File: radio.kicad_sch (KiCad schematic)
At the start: 0 parts

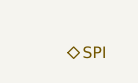
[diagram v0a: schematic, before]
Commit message: Fixed bus names
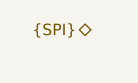
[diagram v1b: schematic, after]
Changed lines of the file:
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@@
 (kicad_sch (version 20211123) (generator eeschema)
   (paper "A4")
-  (hierarchical_label "SPI" (shape bidirectional) (at 25.4 31.75 0)
-    (effects (font (size 1.27 1.27)) (justify left))
+  (hierarchical_label "{SPI}" (shape bidirectional) (at 27.94 29.21 180)
+    (effects (font (size 1.27 1.27)) (justify right))
   )
 )

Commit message: Various updates because I forgot to commit for a while
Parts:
- added AE1: Antenna, Connector_Coaxial:SMA_Molex_73251-2200_Horizontal, symbol Device:Antenna
- added C20: 5.1p, symbol Device:C
- added CM1: 6.8n, symbol Device:L
- added CM2, CM3: 3.3p, symbol Device:C
- added CR1: 3p, symbol Device:C
- added CR2: 1.2p, symbol Device:C
- added L1: 3.3n, symbol Device:L
- added LM1, LM3: 12n, symbol Device:L
- added LM2, LR2: 24n, symbol Device:L
- added LR1: 18n, symbol Device:L
- added Lc1: 120n, symbol Device:L
- added U8: Si4468/7, symbol YAR_Comms:Si4468/7
- added Y2: 30MHz, symbol Device:Crystal
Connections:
- new net: AE1.1 (A), LM3.1
- new net: CM3.1, LM2.1, LM3.2
- new net: CM2.1, LM1.1, LM2.2
- new net: CR1.1, LR1.1, LR2.2, U8.3 (RXn)
- new net: C20.2, Lc1.2, U8.4 (TX)
- new net: C20.1, L1.1
- new net: CM1.2, CR2.2, L1.2, LM1.2, LR2.1
- new net: CR2.1, LR1.2, U8.2 (RXp)
- new net: U8.16 (XOUT), Y2.1
- new net: U8.17 (XIN), Y2.2
- new net +3V3: Lc1.1, U8.6 (Vcc), U8.8 (Vcc)
- new net CS1: U8.15 (CS)
- new net GND: CM1.1, CM2.2, CM3.2, CR1.2, U8.1 (SDN), U8.18 (GND), U8.21 (GND), U8.5 (GND)
- new net Radio: U8.11 (~{IRQ})
- new net Rx: U8.13 (SDO)
- new net SCK: U8.12 (SCLK)
- new net Tx: U8.14 (SDI)
- no-connect marks 0 -> 5
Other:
- note added: "CM is actually an inductor because reasons. I hate it too."
- title: (none) -> Pheonix Radio

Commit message: Added footprint
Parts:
- Y2: footprint (none) -> Oscillator:Oscillator_SMD_Abracon_ASE-4Pin_3.2x2.5mm
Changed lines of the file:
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@@
       (effects (font (size 1.27 1.27)) (justify right))
     )
-    (property "Footprint" "" (id 2) (at 59.69 73.66 0)
+    (property "Footprint" "Oscillator:Oscillator_SMD_Abracon_ASE-4Pin_3.2x2.5mm" (id 2) (at 59.69 73.66 0)
       (effects (font (size 1.27 1.27)) hide)
     )

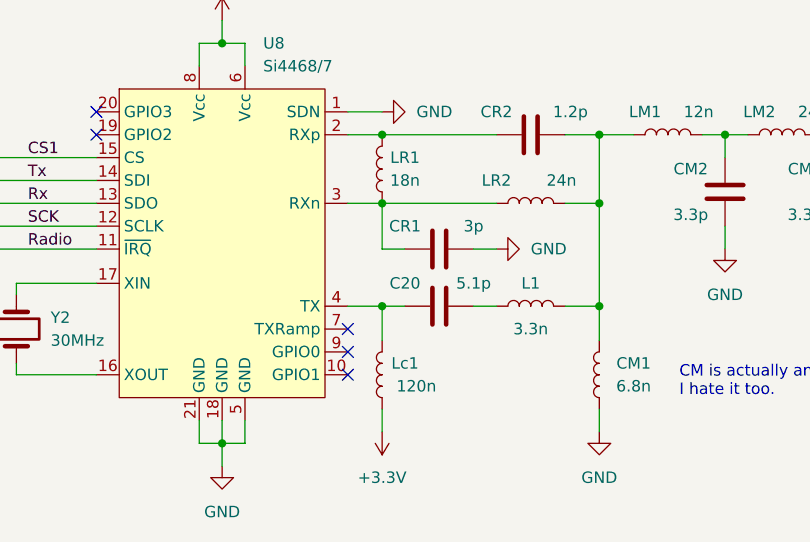
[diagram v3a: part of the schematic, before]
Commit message: Connected the sensors, flash chip, Need to connect the radio and GPS
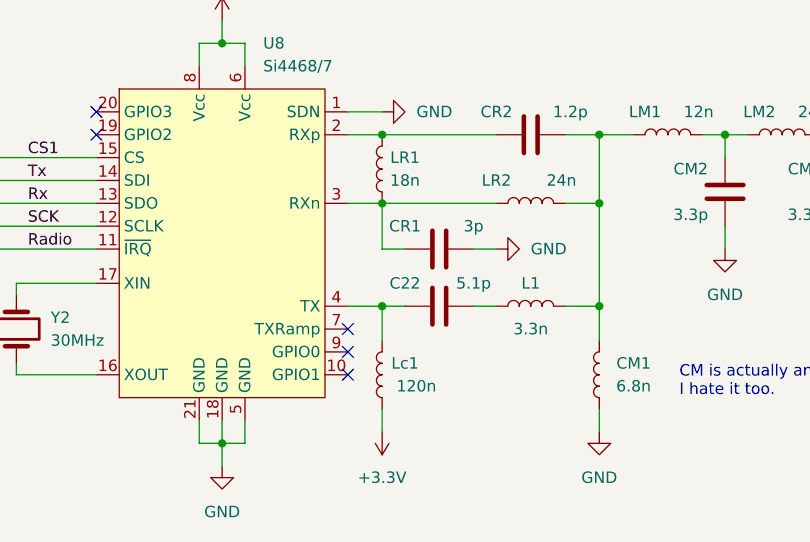
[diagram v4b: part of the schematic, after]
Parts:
- U8: footprint (none) -> YAR_RF:SI4468-A2A-IMR
- renumbered C20 to C22
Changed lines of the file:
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@@
   (symbol (lib_id "power:GND") (at 100.33 49.53 90) (unit 1)
     (in_bom yes) (on_board yes) (fields_autoplaced)
-    (property "Reference" "#PWR045" (id 0) (at 106.68 49.53 0)
+    (property "Reference" "#PWR047" (id 0) (at 106.68 49.53 0)
       (effects (font (size 1.27 1.27)) hide)
     )
@@
   (symbol (lib_id "power:GND") (at 151.13 64.77 0) (unit 1)
     (in_bom yes) (on_board yes) (fields_autoplaced)
-    (property "Reference" "#PWR050" (id 0) (at 151.13 71.12 0)
+    (property "Reference" "#PWR052" (id 0) (at 151.13 71.12 0)
       (effects (font (size 1.27 1.27)) hide)
     )
@@
   (symbol (lib_id "Device:C") (at 106.68 71.12 270) (mirror x) (unit 1)
     (in_bom yes) (on_board yes)
-    (property "Reference" "C20" (id 0) (at 102.87 68.58 90))
+    (property "Reference" "C22" (id 0) (at 102.87 68.58 90))
     (property "Value" "5.1p" (id 1) (at 110.49 68.58 90))
     (property "Footprint" "" (id 2) (at 102.87 70.1548 0)
@@
   (symbol (lib_id "power:GND") (at 138.43 64.77 0) (unit 1)
     (in_bom yes) (on_board yes) (fields_autoplaced)
-    (property "Reference" "#PWR049" (id 0) (at 138.43 71.12 0)
+    (property "Reference" "#PWR051" (id 0) (at 138.43 71.12 0)
       (effects (font (size 1.27 1.27)) hide)
     )
@@
   (symbol (lib_id "power:+3.3V") (at 82.55 39.37 0) (unit 1)
     (in_bom yes) (on_board yes) (fields_autoplaced)
-    (property "Reference" "#PWR043" (id 0) (at 82.55 43.18 0)
+    (property "Reference" "#PWR045" (id 0) (at 82.55 43.18 0)
       (effects (font (size 1.27 1.27)) hide)
     )
@@
   (symbol (lib_id "power:GND") (at 124.46 85.09 0) (unit 1)
     (in_bom yes) (on_board yes) (fields_autoplaced)
-    (property "Reference" "#PWR048" (id 0) (at 124.46 91.44 0)
+    (property "Reference" "#PWR050" (id 0) (at 124.46 91.44 0)
       (effects (font (size 1.27 1.27)) hide)
     )
@@
   (symbol (lib_id "power:+3.3V") (at 100.33 85.09 180) (unit 1)
     (in_bom yes) (on_board yes) (fields_autoplaced)
-    (property "Reference" "#PWR046" (id 0) (at 100.33 81.28 0)
+    (property "Reference" "#PWR048" (id 0) (at 100.33 81.28 0)
       (effects (font (size 1.27 1.27)) hide)
     )
@@
       (effects (font (size 1.27 1.27)) (justify left))
     )
-    (property "Footprint" "" (id 2) (at 82.55 58.42 0)
+    (property "Footprint" "YAR_RF:SI4468-A2A-IMR" (id 2) (at 82.55 58.42 0)
       (effects (font (size 1.27 1.27)) hide)
     )
@@
   (symbol (lib_id "power:GND") (at 82.55 88.9 0) (unit 1)
     (in_bom yes) (on_board yes) (fields_autoplaced)
-    (property "Reference" "#PWR044" (id 0) (at 82.55 95.25 0)
+    (property "Reference" "#PWR046" (id 0) (at 82.55 95.25 0)
       (effects (font (size 1.27 1.27)) hide)
     )
@@
   (symbol (lib_id "power:GND") (at 113.03 64.77 90) (unit 1)
     (in_bom yes) (on_board yes) (fields_autoplaced)
-    (property "Reference" "#PWR047" (id 0) (at 119.38 64.77 0)
-      (effects (font (size 1.27 1.27)) hide)
-    )
+    (property "Reference" "#PWR049" (id 0) (at 119.38 64.77 0)
+      (effects (font (size 1.27 1.27)) hide)
+    )

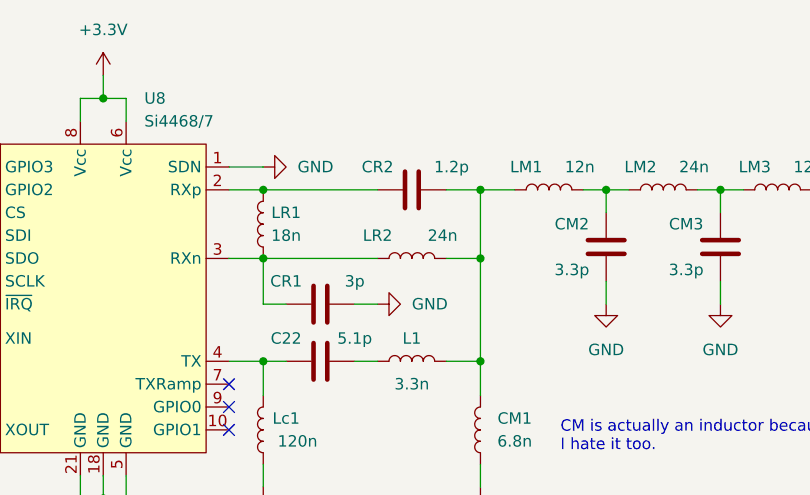
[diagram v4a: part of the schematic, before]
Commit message: Rearrange parts of PCB
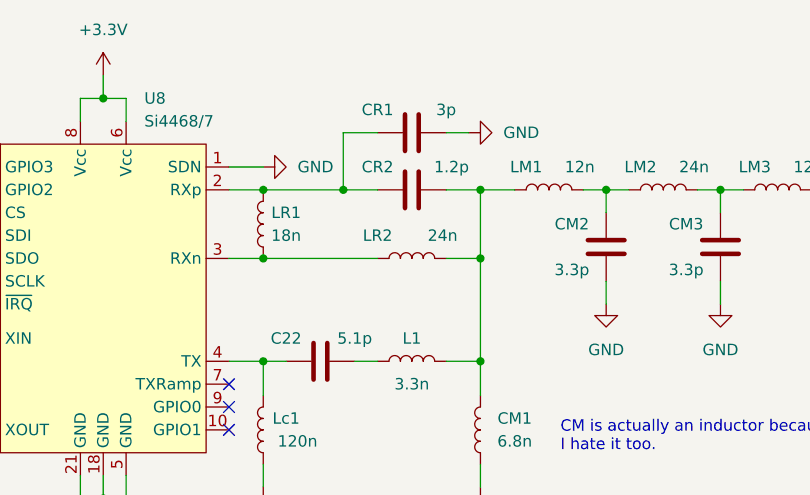
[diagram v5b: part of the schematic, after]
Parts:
- C22, CM1, CM2, CM3, CR1, CR2: footprint (none) -> Capacitor_SMD:C_0603_1608Metric
- L1, LM1, LM2, LM3, LR1, LR2, Lc1: footprint (none) -> Inductor_SMD:L_0603_1608Metric
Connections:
- net at LR1.1, LR2.2, U8.3 (RXn): no longer CR1.1
- net at CR2.1, LR1.2, U8.2 (RXp): now also CR1.1
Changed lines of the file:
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@@
   (junction (at 82.55 86.36) (diameter 0) (color 0 0 0 0)
+  )
+  (junction (at 109.22 52.07) (diameter 0) (color 0 0 0 0)
   )
   (no_connect (at 96.52 78.74))
@@
     (stroke (width 0) (type default) (color 0 0 0 0))
   )
+  (wire (pts (xy 109.22 52.07) (xy 113.03 52.07))
+    (stroke (width 0) (type default) (color 0 0 0 0))
+  )
   (wire (pts (xy 96.52 49.53) (xy 100.33 49.53))
     (stroke (width 0) (type default) (color 0 0 0 0))
@@
     (stroke (width 0) (type default) (color 0 0 0 0))
   )
-  (wire (pts (xy 100.33 52.07) (xy 113.03 52.07))
+  (wire (pts (xy 100.33 52.07) (xy 109.22 52.07))
+    (stroke (width 0) (type default) (color 0 0 0 0))
+  )
+  (wire (pts (xy 109.22 45.72) (xy 113.03 45.72))
     (stroke (width 0) (type default) (color 0 0 0 0))
   )
@@
     (stroke (width 0) (type default) (color 0 0 0 0))
   )
+  (wire (pts (xy 120.65 45.72) (xy 123.19 45.72))
+    (stroke (width 0) (type default) (color 0 0 0 0))
+  )
   (wire (pts (xy 80.01 44.45) (xy 80.01 41.91))
     (stroke (width 0) (type default) (color 0 0 0 0))
   )
-  (wire (pts (xy 100.33 59.69) (xy 100.33 64.77))
-    (stroke (width 0) (type default) (color 0 0 0 0))
-  )
   (wire (pts (xy 96.52 59.69) (xy 100.33 59.69))
     (stroke (width 0) (type default) (color 0 0 0 0))
@@
     (stroke (width 0) (type default) (color 0 0 0 0))
   )
-  (wire (pts (xy 110.49 64.77) (xy 113.03 64.77))
-    (stroke (width 0) (type default) (color 0 0 0 0))
-  )
   (wire (pts (xy 59.69 68.58) (xy 59.69 69.85))
     (stroke (width 0) (type default) (color 0 0 0 0))
@@
     (stroke (width 0) (type default) (color 0 0 0 0))
   )
+  (wire (pts (xy 109.22 45.72) (xy 109.22 52.07))
+    (stroke (width 0) (type default) (color 0 0 0 0))
+  )
   (wire (pts (xy 57.15 59.69) (xy 68.58 59.69))
     (stroke (width 0) (type default) (color 0 0 0 0))
@@
   )
   (bus (pts (xy 50.8 67.31) (xy 54.61 67.31))
-    (stroke (width 0) (type default) (color 0 0 0 0))
-  )
-  (wire (pts (xy 100.33 64.77) (xy 102.87 64.77))
     (stroke (width 0) (type default) (color 0 0 0 0))
   )
@@
     (effects (font (size 1.27 1.27)) (justify right))
   )
+  (symbol (lib_id "Device:C") (at 116.84 45.72 90) (mirror x) (unit 1)
+    (in_bom yes) (on_board yes)
+    (property "Reference" "CR1" (id 0) (at 113.03 43.18 90))
+    (property "Value" "3p" (id 1) (at 120.65 43.18 90))
+    (property "Footprint" "Capacitor_SMD:C_0603_1608Metric" (id 2) (at 120.65 46.6852 0)
+      (effects (font (size 1.27 1.27)) hide)
+    )
+    (property "Datasheet" "~" (id 3) (at 116.84 45.72 0)
+      (effects (font (size 1.27 1.27)) hide)
+    )
+    (pin "1")
+    (pin "2")
+  )
   (symbol (lib_id "Device:Antenna") (at 163.83 44.45 0) (unit 1)
     (in_bom yes) (on_board yes) (fields_autoplaced)
@@
       (effects (font (size 1.27 1.27)) (justify right))
     )
-    (property "Footprint" "" (id 2) (at 144.78 52.07 0)
+    (property "Footprint" "Inductor_SMD:L_0603_1608Metric" (id 2) (at 144.78 52.07 0)
       (effects (font (size 1.27 1.27)) hide)
     )
     (property "Datasheet" "~" (id 3) (at 144.78 52.07 0)
-      (effects (font (size 1.27 1.27)) hide)
-    )
-    (pin "1")
-    (pin "2")
-  )
-  (symbol (lib_id "Device:C") (at 106.68 64.77 90) (mirror x) (unit 1)
-    (in_bom yes) (on_board yes)
-    (property "Reference" "CR1" (id 0) (at 102.87 62.23 90))
-    (property "Value" "3p" (id 1) (at 110.49 62.23 90))
-    (property "Footprint" "" (id 2) (at 110.49 65.7352 0)
-      (effects (font (size 1.27 1.27)) hide)
-    )
-    (property "Datasheet" "~" (id 3) (at 106.68 64.77 0)
       (effects (font (size 1.27 1.27)) hide)
     )
@@
     (property "Reference" "Lc1" (id 0) (at 102.87 77.47 0))
     (property "Value" "120n" (id 1) (at 104.14 80.01 0))
-    (property "Footprint" "" (id 2) (at 100.33 78.74 0)
+    (property "Footprint" "Inductor_SMD:L_0603_1608Metric" (id 2) (at 100.33 78.74 0)
       (effects (font (size 1.27 1.27)) hide)
     )
@@
     (property "Reference" "L1" (id 0) (at 116.84 68.58 90))
     (property "Value" "3.3n" (id 1) (at 116.84 73.66 90))
-    (property "Footprint" "" (id 2) (at 116.84 71.12 0)
+    (property "Footprint" "Inductor_SMD:L_0603_1608Metric" (id 2) (at 116.84 71.12 0)
       (effects (font (size 1.27 1.27)) hide)
     )
@@
       (effects (font (size 1.27 1.27)) (justify right))
     )
-    (property "Footprint" "" (id 2) (at 116.84 59.69 0)
+    (property "Footprint" "Inductor_SMD:L_0603_1608Metric" (id 2) (at 116.84 59.69 0)
       (effects (font (size 1.27 1.27)) hide)
     )
@@
     (property "Reference" "LR1" (id 0) (at 102.87 54.61 0))
     (property "Value" "18n" (id 1) (at 102.87 57.15 0))
-    (property "Footprint" "" (id 2) (at 100.33 55.88 0)
+    (property "Footprint" "Inductor_SMD:L_0603_1608Metric" (id 2) (at 100.33 55.88 0)
       (effects (font (size 1.27 1.27)) hide)
     )
@@
       (effects (font (size 1.27 1.27)) (justify right))
     )
-    (property "Footprint" "" (id 2) (at 157.48 52.07 0)
+    (property "Footprint" "Inductor_SMD:L_0603_1608Metric" (id 2) (at 157.48 52.07 0)
       (effects (font (size 1.27 1.27)) hide)
     )
@@
     (property "Reference" "C22" (id 0) (at 102.87 68.58 90))
     (property "Value" "5.1p" (id 1) (at 110.49 68.58 90))
-    (property "Footprint" "" (id 2) (at 102.87 70.1548 0)
+    (property "Footprint" "Capacitor_SMD:C_0603_1608Metric" (id 2) (at 102.87 70.1548 0)
       (effects (font (size 1.27 1.27)) hide)
     )
@@
     (property "Reference" "CM1" (id 0) (at 128.27 77.47 0))
     (property "Value" "6.8n" (id 1) (at 128.27 80.01 0))
-    (property "Footprint" "" (id 2) (at 124.46 78.74 0)
+    (property "Footprint" "Capacitor_SMD:C_0603_1608Metric" (id 2) (at 124.46 78.74 0)
       (effects (font (size 1.27 1.27)) hide)
     )
@@
       (effects (font (size 1.27 1.27)) (justify right))
     )
-    (property "Footprint" "" (id 2) (at 132.08 52.07 0)
+    (property "Footprint" "Inductor_SMD:L_0603_1608Metric" (id 2) (at 132.08 52.07 0)
       (effects (font (size 1.27 1.27)) hide)
     )
@@
     (property "Reference" "CM2" (id 0) (at 134.62 55.88 0))
     (property "Value" "3.3p" (id 1) (at 134.62 60.96 0))
-    (property "Footprint" "" (id 2) (at 137.4648 62.23 0)
+    (property "Footprint" "Capacitor_SMD:C_0603_1608Metric" (id 2) (at 137.4648 62.23 0)
       (effects (font (size 1.27 1.27)) hide)
     )
@@
     (pin "1")
     (pin "2")
+  )
+  (symbol (lib_id "power:GND") (at 123.19 45.72 90) (unit 1)
+    (in_bom yes) (on_board yes) (fields_autoplaced)
+    (property "Reference" "#PWR0101" (id 0) (at 129.54 45.72 0)
+      (effects (font (size 1.27 1.27)) hide)
+    )
+    (property "Value" "GND" (id 1) (at 127 45.7199 90)
+      (effects (font (size 1.27 1.27)) (justify right))
+    )
+    (property "Footprint" "" (id 2) (at 123.19 45.72 0)
+      (effects (font (size 1.27 1.27)) hide)
+    )
+    (property "Datasheet" "" (id 3) (at 123.19 45.72 0)
+      (effects (font (size 1.27 1.27)) hide)
+    )
+    (pin "1")
   )
   (symbol (lib_id "power:GND") (at 124.46 85.09 0) (unit 1)
@@
     (property "Reference" "CM3" (id 0) (at 147.32 55.88 0))
     (property "Value" "3.3p" (id 1) (at 147.32 60.96 0))
-    (property "Footprint" "" (id 2) (at 150.1648 62.23 0)
+    (property "Footprint" "Capacitor_SMD:C_0603_1608Metric" (id 2) (at 150.1648 62.23 0)
       (effects (font (size 1.27 1.27)) hide)
     )
@@
       (effects (font (size 1.27 1.27)) (justify left))
     )
-    (property "Footprint" "" (id 2) (at 120.65 53.0352 0)
+    (property "Footprint" "Capacitor_SMD:C_0603_1608Metric" (id 2) (at 120.65 53.0352 0)
       (effects (font (size 1.27 1.27)) hide)
     )
@@
       (effects (font (size 1.27 1.27)) hide)
     )
-    (pin "1")
-  )
-  (symbol (lib_id "power:GND") (at 113.03 64.77 90) (unit 1)
-    (in_bom yes) (on_board yes) (fields_autoplaced)
-    (property "Reference" "#PWR049" (id 0) (at 119.38 64.77 0)
-      (effects (font (size 1.27 1.27)) hide)
-    )
-    (property "Value" "GND" (id 1) (at 116.84 64.7699 90)
-      (effects (font (size 1.27 1.27)) (justify right))
-    )
-    (property "Footprint" "" (id 2) (at 113.03 64.77 0)
-      (effects (font (size 1.27 1.27)) hide)
-    )
-    (property "Datasheet" "" (id 3) (at 113.03 64.77 0)
-      (effects (font (size 1.27 1.27)) hide)
-    )

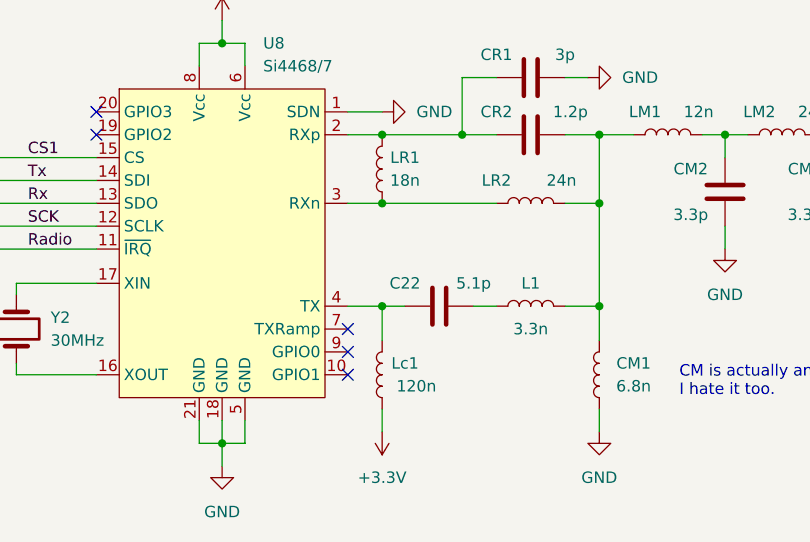
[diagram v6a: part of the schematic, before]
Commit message: Added polyfuse
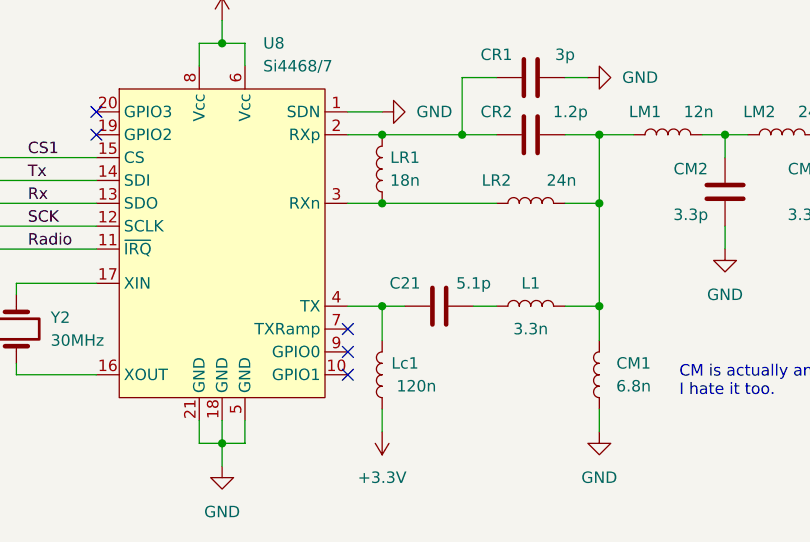
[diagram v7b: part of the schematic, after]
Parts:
- renumbered C22 to C21
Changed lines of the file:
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@@
   (symbol (lib_id "power:GND") (at 100.33 49.53 90) (unit 1)
     (in_bom yes) (on_board yes) (fields_autoplaced)
-    (property "Reference" "#PWR047" (id 0) (at 106.68 49.53 0)
+    (property "Reference" "#PWR045" (id 0) (at 106.68 49.53 0)
       (effects (font (size 1.27 1.27)) hide)
     )
@@
   (symbol (lib_id "power:GND") (at 151.13 64.77 0) (unit 1)
     (in_bom yes) (on_board yes) (fields_autoplaced)
-    (property "Reference" "#PWR052" (id 0) (at 151.13 71.12 0)
+    (property "Reference" "#PWR050" (id 0) (at 151.13 71.12 0)
       (effects (font (size 1.27 1.27)) hide)
     )
@@
   (symbol (lib_id "Device:C") (at 106.68 71.12 270) (mirror x) (unit 1)
     (in_bom yes) (on_board yes)
-    (property "Reference" "C22" (id 0) (at 102.87 68.58 90))
+    (property "Reference" "C21" (id 0) (at 102.87 68.58 90))
     (property "Value" "5.1p" (id 1) (at 110.49 68.58 90))
     (property "Footprint" "Capacitor_SMD:C_0603_1608Metric" (id 2) (at 102.87 70.1548 0)
@@
   (symbol (lib_id "power:GND") (at 138.43 64.77 0) (unit 1)
     (in_bom yes) (on_board yes) (fields_autoplaced)
-    (property "Reference" "#PWR051" (id 0) (at 138.43 71.12 0)
+    (property "Reference" "#PWR049" (id 0) (at 138.43 71.12 0)
       (effects (font (size 1.27 1.27)) hide)
     )
@@
   (symbol (lib_id "power:+3.3V") (at 82.55 39.37 0) (unit 1)
     (in_bom yes) (on_board yes) (fields_autoplaced)
-    (property "Reference" "#PWR045" (id 0) (at 82.55 43.18 0)
+    (property "Reference" "#PWR043" (id 0) (at 82.55 43.18 0)
       (effects (font (size 1.27 1.27)) hide)
     )
@@
   (symbol (lib_id "power:GND") (at 123.19 45.72 90) (unit 1)
     (in_bom yes) (on_board yes) (fields_autoplaced)
-    (property "Reference" "#PWR0101" (id 0) (at 129.54 45.72 0)
+    (property "Reference" "#PWR047" (id 0) (at 129.54 45.72 0)
       (effects (font (size 1.27 1.27)) hide)
     )
@@
   (symbol (lib_id "power:GND") (at 124.46 85.09 0) (unit 1)
     (in_bom yes) (on_board yes) (fields_autoplaced)
-    (property "Reference" "#PWR050" (id 0) (at 124.46 91.44 0)
+    (property "Reference" "#PWR048" (id 0) (at 124.46 91.44 0)
       (effects (font (size 1.27 1.27)) hide)
     )
@@
   (symbol (lib_id "power:+3.3V") (at 100.33 85.09 180) (unit 1)
     (in_bom yes) (on_board yes) (fields_autoplaced)
-    (property "Reference" "#PWR048" (id 0) (at 100.33 81.28 0)
+    (property "Reference" "#PWR046" (id 0) (at 100.33 81.28 0)
       (effects (font (size 1.27 1.27)) hide)
     )
@@
   (symbol (lib_id "power:GND") (at 82.55 88.9 0) (unit 1)
     (in_bom yes) (on_board yes) (fields_autoplaced)
-    (property "Reference" "#PWR046" (id 0) (at 82.55 95.25 0)
-      (effects (font (size 1.27 1.27)) hide)
-    )
+    (property "Reference" "#PWR044" (id 0) (at 82.55 95.25 0)
+      (effects (font (size 1.27 1.27)) hide)
+    )
